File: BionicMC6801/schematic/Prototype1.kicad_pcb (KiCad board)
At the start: 2 copper layers, 48.3 x 71.1 mm, 11 parts, among them J1 BionicConnector, U1 MC6801P, U2 74HCT126

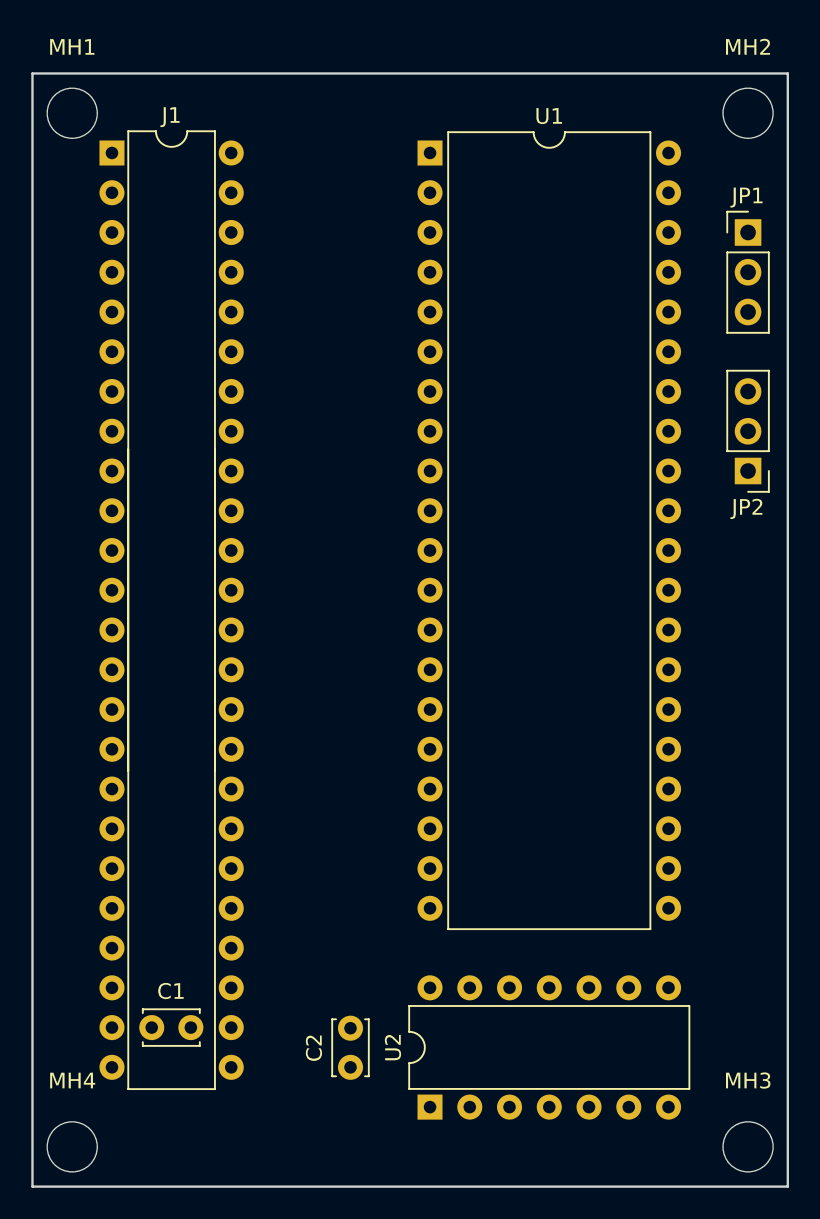
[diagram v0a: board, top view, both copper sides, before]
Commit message: Fix Bionic connector pin outs
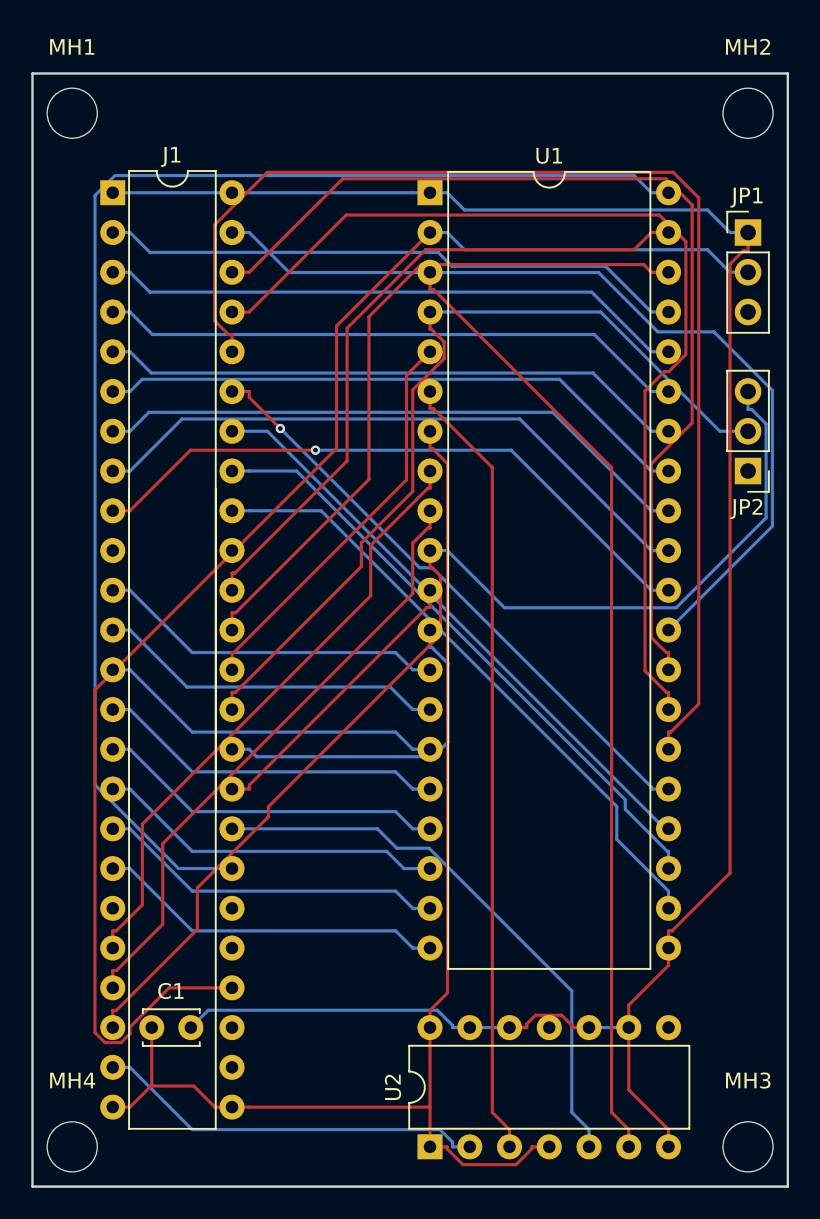
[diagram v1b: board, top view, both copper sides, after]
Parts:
- removed C2: 0.1u, Capacitor_THT:C_Disc_D3.4mm_W2.1mm_P2.50mm
- moved J1 2.54 mm to (103.6, 75.1)
- moved U1 2.54 mm to (123.9, 75.1)
- moved U2 2.54 mm to (123.9, 136.0)
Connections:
- net Net-(J1-Pad28) renamed /P55
- J1 pad 11: /P20 -> /P30
- J1 pad 12: /P21 -> /P31
- J1 pad 13: /P22 -> /P32
- J1 pad 14: /P23 -> /P33
- J1 pad 15: /P24 -> /P34
- J1 pad 16: /P25 -> /P35
- J1 pad 17: /P26 -> /P36
- J1 pad 18: /P27 -> /P37
- J1 pad 23: VCC -> /P53
- J1 pad 40: /P37 -> /P27
- J1 pad 41: /P36 -> /P26
- J1 pad 42: /P35 -> /P25
- J1 pad 43: /P34 -> /P24
- J1 pad 44: /P33 -> /P23
- J1 pad 45: /P32 -> /P22
- J1 pad 46: /P31 -> /P21
- J1 pad 47: /P30 -> /P20
- JP2 pad 2: /P51 -> /P43
- JP2 pad 3: /P43 -> /P52
- U2 pad 2: VCC -> /P53
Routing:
- net GND: track 0.00 -> 134.4 mm
- net /P55: track 0.00 -> 92.1 mm
- net /P47: track 0.00 -> 86.3 mm
- net VCC: track 0.00 -> 80.6 mm
- net /P23: track 0.00 -> 77.8 mm
- net /P52: track 0.00 -> 73.7 mm
- net /P22: track 0.00 -> 64.1 mm
- net /P21: track 0.00 -> 63.9 mm
- net Net-(U1-Pad3): track 0.00 -> 61.3 mm
- net /P20: track 0.00 -> 56.8 mm
- net /P43: track 0.00 -> 55.0 mm
- net /#RESET: track 0.00 -> 50.5 mm
- net /P41: track 0.00 -> 44.5 mm
- net /P40: track 0.00 -> 43.0 mm
- net /P17: track 0.00 -> 40.8 mm, vias 0 -> 1
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
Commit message: Migrate to KiCad 6.0
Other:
- net class Default removed
